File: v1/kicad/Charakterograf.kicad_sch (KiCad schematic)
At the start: 0 parts

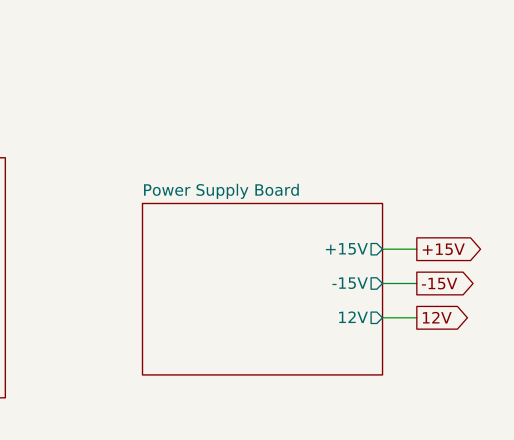
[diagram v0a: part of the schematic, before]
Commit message: Changed the file structure
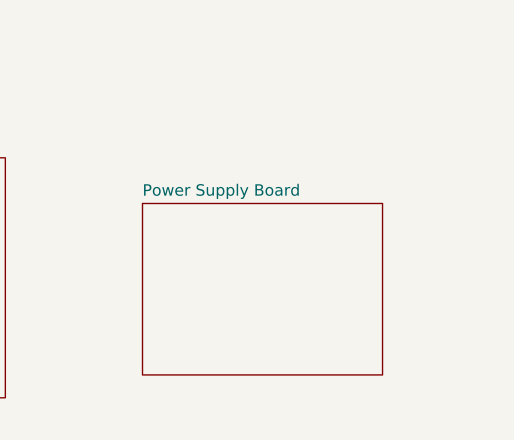
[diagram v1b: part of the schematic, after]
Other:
- sheet Power Supply Board ports: added none; removed +15V, -15V, 12V
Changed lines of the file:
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@@
-		)
-	)
-	(wire
-		(pts
-			(xy 148.59 63.5) (xy 144.78 63.5)
-		)
-		(stroke
-			(width 0)
-			(type default)
-		)
-	)
-	(wire
-		(pts
-			(xy 144.78 59.69) (xy 148.59 59.69)
-		)
-		(stroke
-			(width 0)
-			(type default)
-		)
-	)
-	(wire
-		(pts
-			(xy 144.78 67.31) (xy 148.59 67.31)
-		)
-		(stroke
-			(width 0)
-			(type default)
-		)
-	)
-	(global_label "12V"
-		(shape output)
-		(at 148.59 67.31 0)
-		(fields_autoplaced yes)
-		(effects
-			(font
-				(size 1.27 1.27)
-			)
-			(justify left)
-		)
-		(property "Intersheetrefs" "${INTERSHEET_REFS}"
-			(at 155.0828 67.31 0)
-			(hide yes)
-			(show_name no)
-			(do_not_autoplace no)
-			(effects
-				(font
-					(size 1.27 1.27)
-				)
-				(justify left)
-			)
-		)
-	)
-	(global_label "+15V"
-		(shape output)
-		(at 148.59 59.69 0)
-		(fields_autoplaced yes)
-		(effects
-			(font
-				(size 1.27 1.27)
-			)
-			(justify left)
-		)
-		(property "Intersheetrefs" "${INTERSHEET_REFS}"
-			(at 156.6552 59.69 0)
-			(hide yes)
-			(show_name no)
-			(do_not_autoplace no)
-			(effects
-				(font
-					(size 1.27 1.27)
-				)
-				(justify left)
-			)
-		)
-	)
-	(global_label "-15V"
-		(shape output)
-		(at 148.59 63.5 0)
-		(fields_autoplaced yes)
-		(effects
-			(font
-				(size 1.27 1.27)
-			)
-			(justify left)
-		)
-		(property "Intersheetrefs" "${INTERSHEET_REFS}"
-			(at 156.6552 63.5 0)
-			(hide yes)
-			(show_name no)
-			(do_not_autoplace no)
-			(effects
-				(font
-					(size 1.27 1.27)
-				)
-				(justify left)
-			)
 		)
 	)
@@
 			)
 		)
-		(pin "+15V" output
-			(at 144.78 59.69 0)
-			(effects
-				(font
-					(size 1.27 1.27)
-				)
-				(justify right)
-			)
-		)
-		(pin "-15V" output
-			(at 144.78 63.5 0)
-			(effects
-				(font
-					(size 1.27 1.27)
-				)
-				(justify right)
-			)
-		)
-		(pin "12V" output
-			(at 144.78 67.31 0)
-			(effects
-				(font
-					(size 1.27 1.27)
-				)
-				(justify right)
-			)
-		)

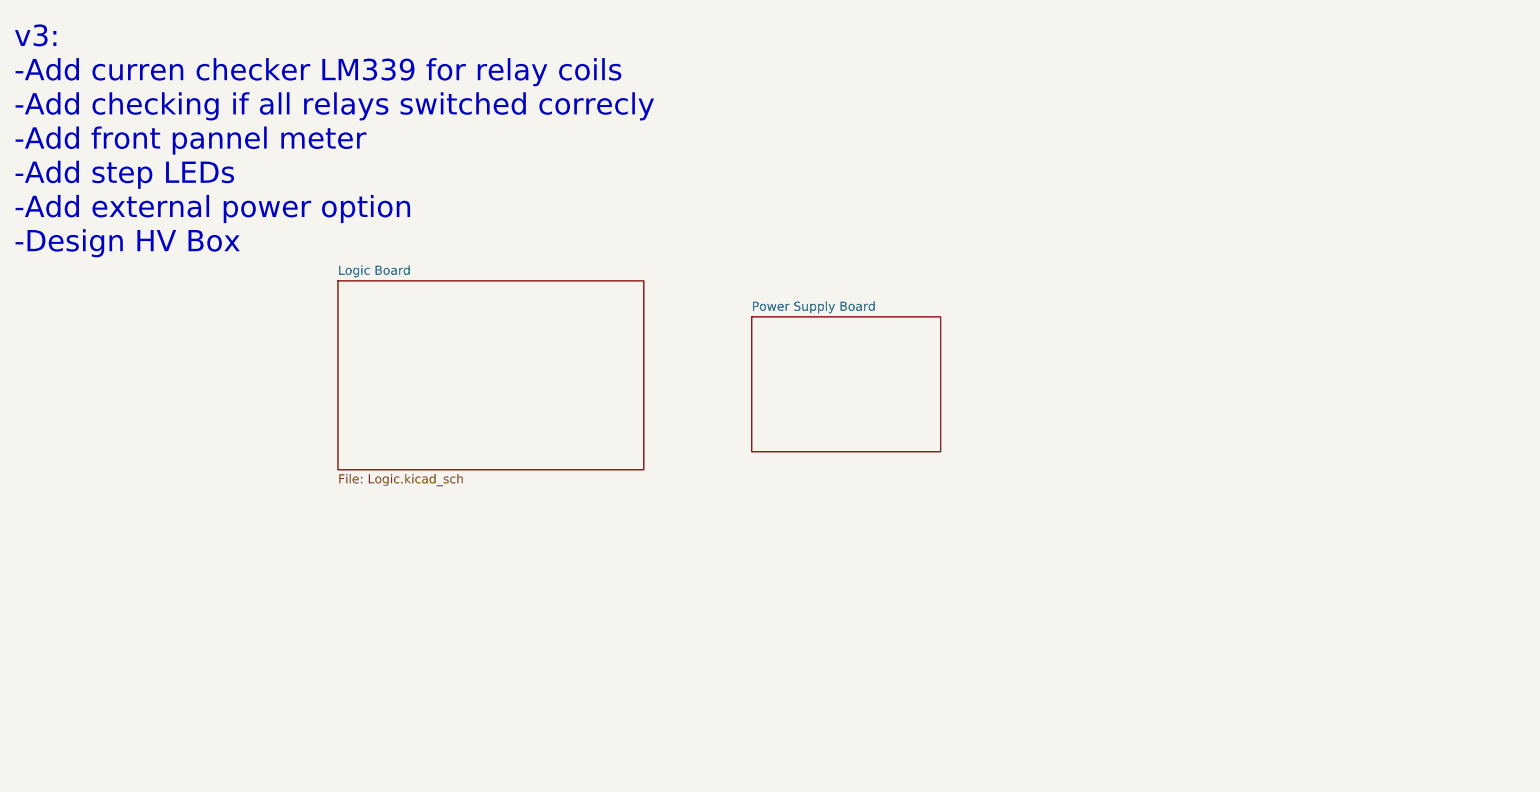
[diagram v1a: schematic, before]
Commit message: Added a DUT board, changed the output connectors , added test hooks, removed unnecessary switches, added FET support
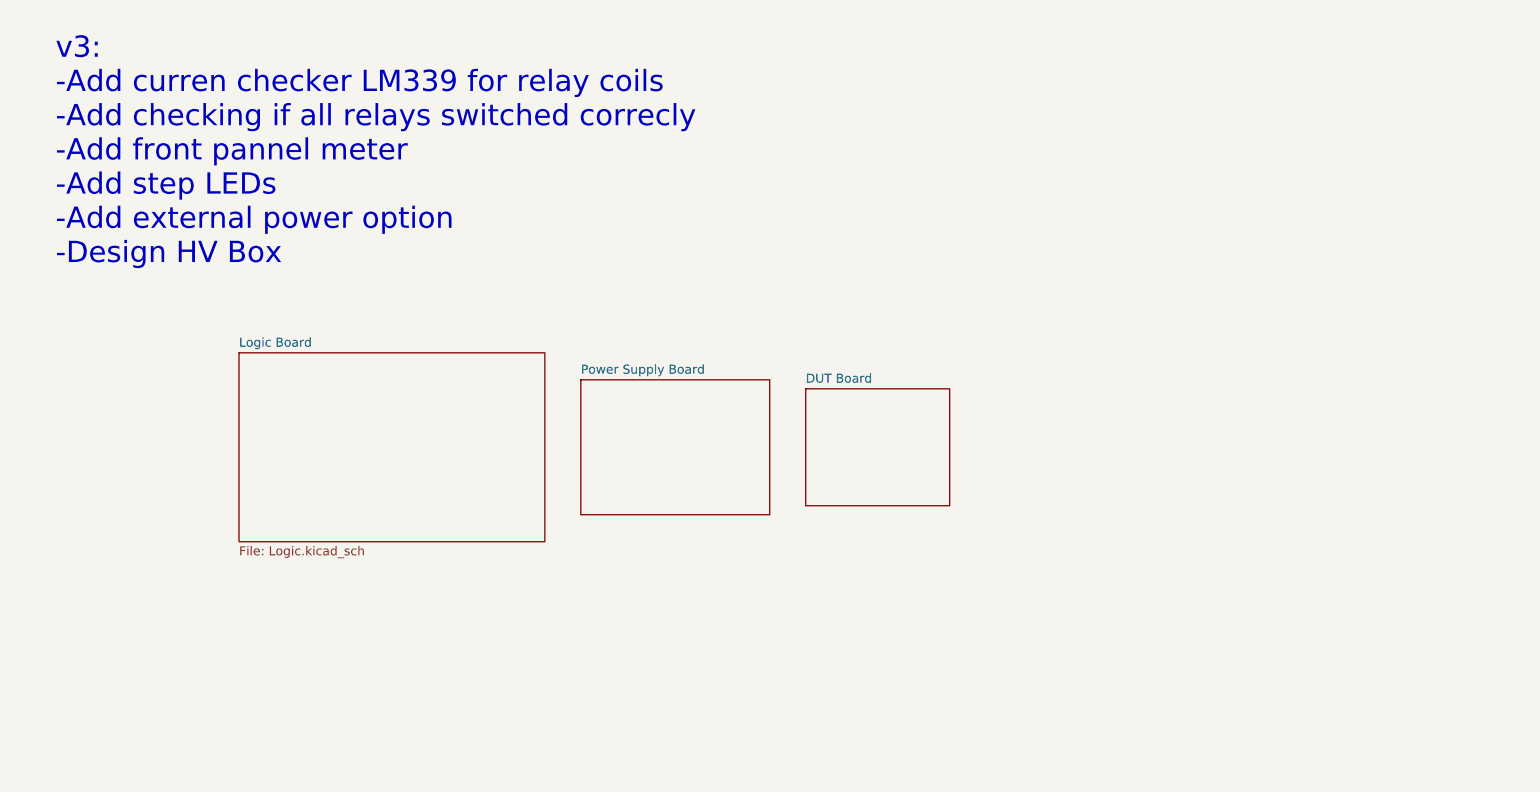
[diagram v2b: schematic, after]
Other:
- added sheet DUT Board (DUT.kicad_sch)
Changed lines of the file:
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@@
 	(text "v3:\n-Add curren checker LM339 for relay coils\n-Add checking if all relays switched correcly\n-Add front pannel meter\n-Add step LEDs\n-Add external power option\n-Design HV Box"
 		(exclude_from_sim no)
-		(at 13.97 29.718 0)
+		(at 19.812 31.242 0)
 		(effects
 			(font
@@
 	)
 	(sheet
-		(at 59.69 49.53)
+		(at 45.72 59.69)
 		(size 43.18 26.67)
 		(exclude_from_sim no)
@@
 		)
 		(property "Sheetname" "Logic Board"
-			(at 59.69 48.8184 0)
+			(at 45.72 58.9784 0)
 			(show_name no)
 			(do_not_autoplace no)
@@
 		)
 		(property "Sheetfile" "Logic.kicad_sch"
-			(at 59.69 76.7846 0)
+			(at 45.72 86.9446 0)
 			(show_name no)
 			(do_not_autoplace no)
@@
 	)
 	(sheet
-		(at 118.11 54.61)
+		(at 93.98 63.5)
 		(size 26.67 19.05)
 		(exclude_from_sim no)
@@
 		)
 		(property "Sheetname" "Power Supply Board"
-			(at 118.11 53.8984 0)
+			(at 93.98 62.7884 0)
 			(show_name no)
 			(do_not_autoplace no)
@@
 		)
 		(property "Sheetfile" "power_supply.kicad_sch"
-			(at 118.11 74.2446 0)
+			(at 93.98 83.1346 0)
 			(hide yes)
 			(show_name no)
@@
 				)
 			)
+		)
+	)
+	(sheet
+		(at 125.73 64.77)
+		(size 20.32 16.51)
+		(exclude_from_sim no)
+		(in_bom yes)
+		(on_board yes)
+		(dnp no)
+		(fields_autoplaced yes)
+		(stroke
+			(width 0.1524)
+			(type solid)
+		)
+		(fill
+			(color 0 0 0 0)
+		)
+		(property "Sheetname" "DUT Board"
+			(at 125.73 64.0584 0)
+			(show_name no)
+			(do_not_autoplace no)
+			(effects
+				(font
+					(size 1.27 1.27)
+				)
+				(justify left bottom)
+			)
+		)
+		(property "Sheetfile" "DUT.kicad_sch"
+			(at 125.73 81.8646 0)
+			(hide yes)
+			(show_name no)
+			(do_not_autoplace no)
+			(effects
+				(font
+					(size 1.27 1.27)
+				)
+				(justify left top)
+			)
+		)
+		(instances
+			(project "Charakterograf"
+				(path "/d7a5a570-e509-45ae-a7d3-ba88e6083368"
+					(page "5")
+				)
+			)

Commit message: Adding KiKit multiboarding
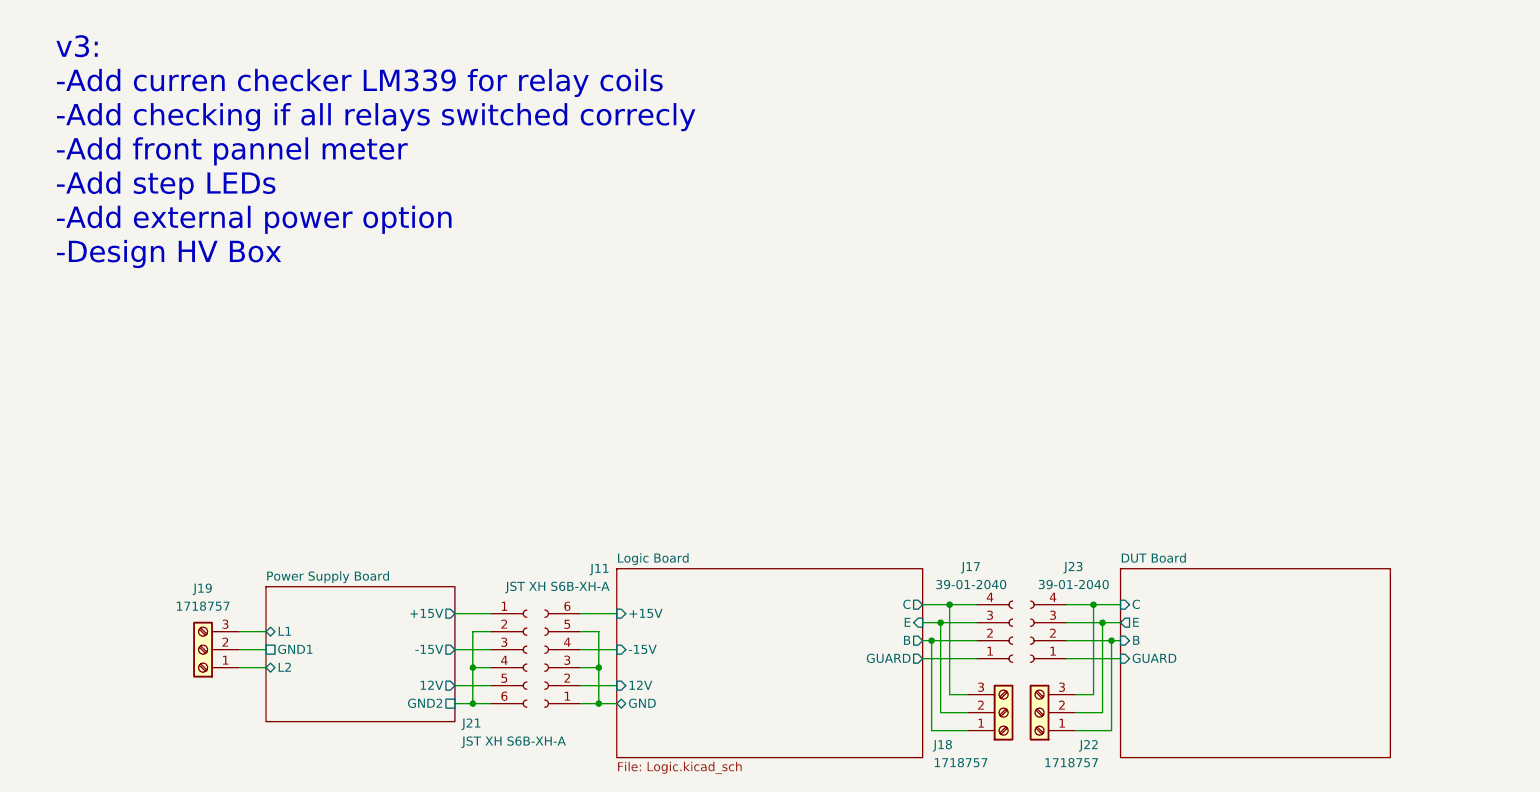
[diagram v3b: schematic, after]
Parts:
- added J11, J21: JST XH S6B-XH-A, Connector_JST:JST_XH_S6B-XH-A_1x06_P2.50mm_Horizontal, symbol Connector:Conn_01x06_Socket
- added J17, J23: 39-01-2040, symbol Connector:Conn_01x04_Socket
- added J18, J19, J22: 1718757, symbol Connector:Screw_Terminal_01x03
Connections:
- new net DUT Board/B: J22.1 (Pin_1), J23.2 (Pin_2)
- new net DUT Board/C: J22.3 (Pin_3), J23.4 (Pin_4)
- new net DUT Board/E: J22.2 (Pin_2), J23.3 (Pin_3)
- new net DUT Board/GUARD: J23.1 (Pin_1)
- new net Logic Board/+15V: J11.6 (Pin_6)
- new net Logic Board/-15V: J11.4 (Pin_4)
- new net Logic Board/12V: J11.2 (Pin_2)
- new net Logic Board/B: J17.2 (Pin_2), J18.1 (Pin_1)
- new net Logic Board/C: J17.4 (Pin_4), J18.3 (Pin_3)
- new net Logic Board/E: J17.3 (Pin_3), J18.2 (Pin_2)
- new net Logic Board/GND: J11.1 (Pin_1), J11.3 (Pin_3), J11.5 (Pin_5)
- new net Logic Board/GUARD: J17.1 (Pin_1)
- new net Power Supply Board/+15V: J21.1 (Pin_1)
- new net Power Supply Board/-15V: J21.3 (Pin_3)
- new net Power Supply Board/12V: J21.5 (Pin_5)
- new net Power Supply Board/GND1: J19.2 (Pin_2)
- new net Power Supply Board/GND2: J21.2 (Pin_2), J21.4 (Pin_4), J21.6 (Pin_6)
- new net Power Supply Board/L1: J19.3 (Pin_3)
- new net Power Supply Board/L2: J19.1 (Pin_1)
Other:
- sheet DUT Board ports: added B, C, E, GUARD; removed none
- sheet Logic Board ports: added +15V, -15V, 12V, B, C, E, GND, GUARD; removed none
- sheet Power Supply Board ports: added +15V, -15V, 12V, GND1, GND2, L1, L2; removed none

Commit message: Fixed mistakes with the polarity of some caps
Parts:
- J17, J23: value 39-01-2040 -> 39-28-1043
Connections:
- net DUT Board/B: now also J22.3 (Pin_3), J23.3 (Pin_3); no longer J22.1 (Pin_1), J23.2 (Pin_2)
- net DUT Board/C: now also J22.1 (Pin_1), J23.1 (Pin_1); no longer J22.3 (Pin_3), J23.4 (Pin_4)
- net DUT Board/E: now also J23.2 (Pin_2); no longer J23.3 (Pin_3)
- net DUT Board/GUARD: now also J23.4 (Pin_4); no longer J23.1 (Pin_1)
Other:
- moved on the sheet: J11, J17, J18, J19, J21, J22, J23

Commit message: Fixed mistakes and made making a BOM easier
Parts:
- J11, J21: footprint Connector_JST:JST_XH_S6B-XH-A_1x06_P2.50mm_Horizontal -> (none); Spend (none) -> $$$
- J17, J18, J19, J22, J23: Spend (none) -> $$$
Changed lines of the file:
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@@
 			)
 		)
-		(property "Footprint" "Connector_JST:JST_XH_S6B-XH-A_1x06_P2.50mm_Horizontal"
+		(property "Footprint" ""
 			(at 107.95 104.14 0)
 			(hide yes)
@@
 		)
 		(property "Description" ""
+			(at 107.95 104.14 0)
+			(hide yes)
+			(show_name no)
+			(do_not_autoplace no)
+			(effects
+				(font
+					(size 1.27 1.27)
+				)
+			)
+		)
+		(property "Spend" "$$$"
 			(at 107.95 104.14 0)
 			(hide yes)
@@
 			)
 		)
-		(property "Footprint" "Connector_JST:JST_XH_S6B-XH-A_1x06_P2.50mm_Horizontal"
+		(property "Footprint" ""
 			(at 105.41 101.6 0)
 			(hide yes)
@@
 		)
 		(property "Description" ""
+			(at 105.41 101.6 0)
+			(hide yes)
+			(show_name no)
+			(do_not_autoplace no)
+			(effects
+				(font
+					(size 1.27 1.27)
+				)
+			)
+		)
+		(property "Spend" "$$$"
+			(at 105.41 101.6 0)
+			(hide yes)
+			(show_name no)
+			(do_not_autoplace no)
+			(effects
+				(font
+					(size 1.27 1.27)
+				)
+			)
+		)
+		(property "Field6" ""
 			(at 105.41 101.6 0)
 			(hide yes)
@@
 			)
 		)
-		(property "Description" "Generic screw terminal, single row, 01x03, script generated (kicad-library-utils/schlib/autogen/connector/)"
+		(property "Description" ""
+			(at 172.72 110.49 0)
+			(hide yes)
+			(show_name no)
+			(do_not_autoplace no)
+			(effects
+				(font
+					(size 1.27 1.27)
+				)
+			)
+		)
+		(property "Spend" "$$$"
 			(at 172.72 110.49 0)
 			(hide yes)
@@
 			)
 		)
-		(property "Description" "Generic connector, single row, 01x04, script generated"
+		(property "Description" ""
+			(at 176.53 97.79 0)
+			(hide yes)
+			(show_name no)
+			(do_not_autoplace no)
+			(effects
+				(font
+					(size 1.27 1.27)
+				)
+			)
+		)
+		(property "Spend" "$$$"
 			(at 176.53 97.79 0)
 			(hide yes)
@@
 		)
 		(property "Description" ""
+			(at 59.69 101.6 0)
+			(hide yes)
+			(show_name no)
+			(do_not_autoplace no)
+			(effects
+				(font
+					(size 1.27 1.27)
+				)
+			)
+		)
+		(property "Spend" "$$$"
 			(at 59.69 101.6 0)
 			(hide yes)
@@
 			)
 		)
-		(property "Description" "Generic connector, single row, 01x04, script generated"
+		(property "Description" ""
+			(at 173.99 100.33 0)
+			(hide yes)
+			(show_name no)
+			(do_not_autoplace no)
+			(effects
+				(font
+					(size 1.27 1.27)
+				)
+			)
+		)
+		(property "Spend" "$$$"
 			(at 173.99 100.33 0)
 			(hide yes)
@@
 			)
 		)
-		(property "Description" "Generic screw terminal, single row, 01x03, script generated (kicad-library-utils/schlib/autogen/connector/)"
+		(property "Description" ""
+			(at 177.8 110.49 0)
+			(hide yes)
+			(show_name no)
+			(do_not_autoplace no)
+			(effects
+				(font
+					(size 1.27 1.27)
+				)
+			)
+		)
+		(property "Spend" "$$$"
 			(at 177.8 110.49 0)
 			(hide yes)
@@
 			)
 		)
-		(pin "GND" bidirectional
+		(pin "GND" passive
 			(at 118.11 109.22 180)
 			(effects
